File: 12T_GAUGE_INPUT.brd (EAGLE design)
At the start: 70.8 x 63.2 mm, 111 parts, among them P1_WP 10k, P2_WP 10k, P3_WP 10k

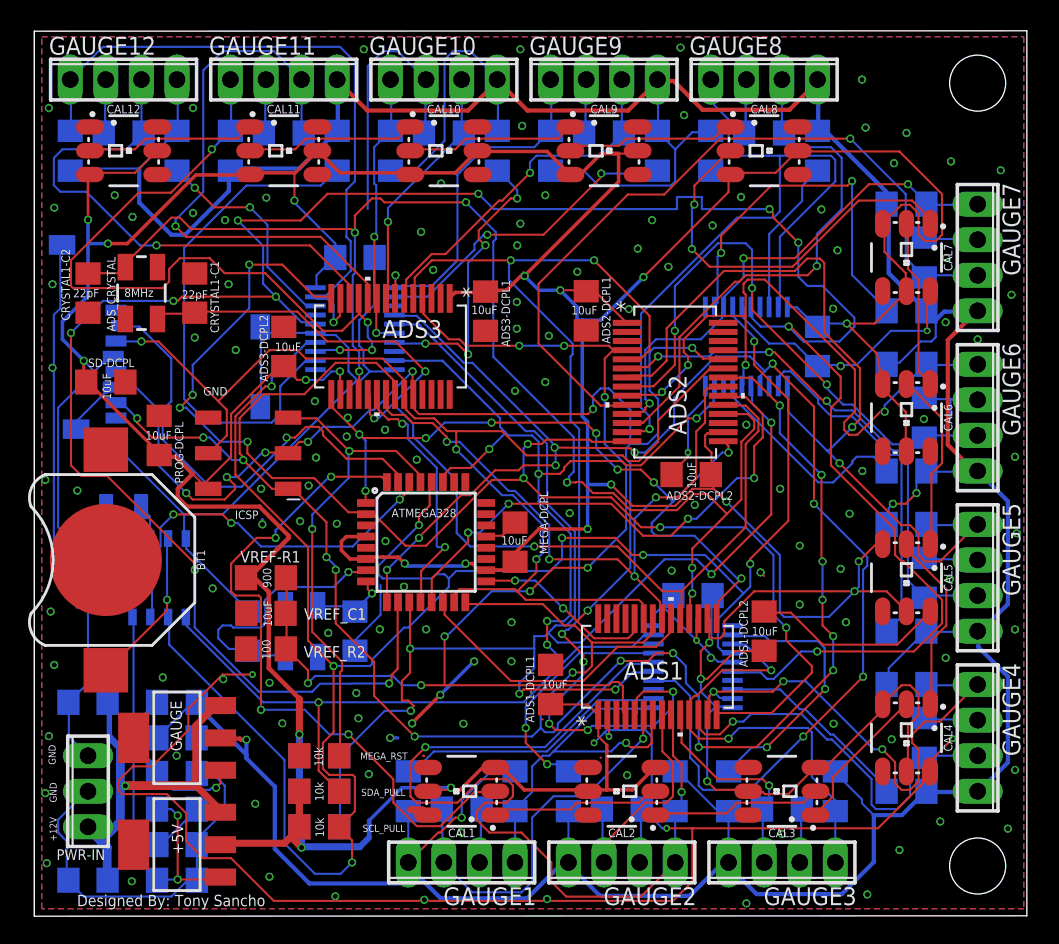
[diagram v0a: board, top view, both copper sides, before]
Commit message: Readability, and made board smaller (again)
Schematic: Moved things around to make it more easily read

Board: Moved things around to shrink the board and increase the ground plane area
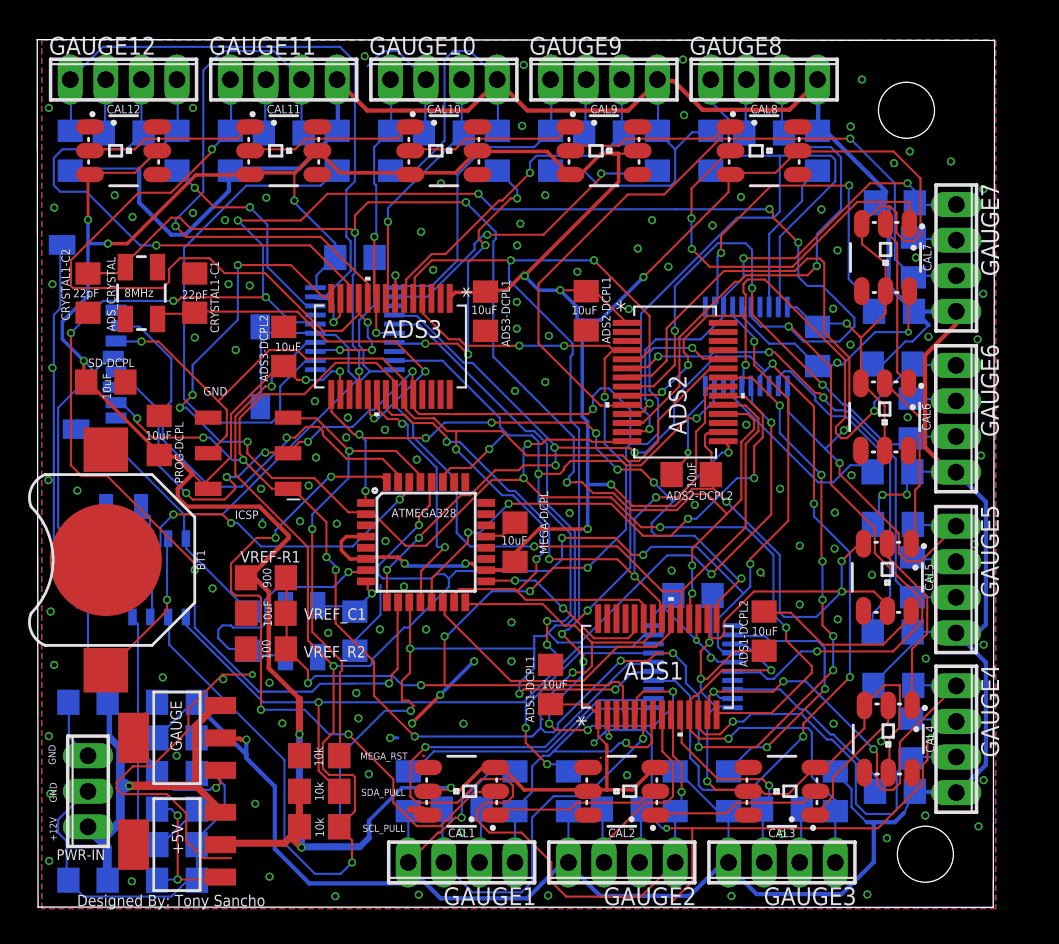
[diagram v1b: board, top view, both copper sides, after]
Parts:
- moved CAL6 1.56 mm to (60.7, 35.6)
- moved GAUGE5 1.55 mm to (65.8, 24.0)
- moved GAUGE6 1.54 mm to (65.8, 35.5)
- moved GAUGE4 1.53 mm to (65.8, 12.6)
- moved GAUGE7 1.52 mm to (65.8, 47.0)
- moved CAL7 1.49 mm to (60.7, 47.0)
- moved CAL5 1.37 mm to (60.9, 24.2)
- moved CAL4 1.30 mm to (60.9, 12.6)
- moved B6-R2 1.00 mm to (61.2, 31.7)
- moved B5-R2 0.99 mm to (61.2, 20.3)
- moved B6R3 0.98 mm to (61.2, 39.4)
- moved B4-R1 0.97 mm to (62.5, 12.7)
- moved B5R3 0.97 mm to (61.3, 27.9)
- moved B6-R1 0.94 mm to (62.6, 35.5)
- moved B4R3 0.94 mm to (61.3, 16.4)
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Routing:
- net GND: track 372.1 -> 316.9 mm, vias 133 -> 136
- net +5V: track 479.6 -> 474.4 mm
- net POT_SELECT_1: track 178.9 -> 174.2 mm
- net B4-_P1W3: track 36.0 -> 33.4 mm
- net B5-_P2W0: track 60.1 -> 57.6 mm
- net B5+: track 38.1 -> 36.4 mm
- net +12V: track 30.0 -> 31.6 mm
- net B6+: track 41.5 -> 39.9 mm
- net P2B1: track 15.6 -> 14.3 mm
- net POT_SELECT_0: track 106.0 -> 105.0 mm
- net B7+: track 55.0 -> 54.0 mm
- net P2B2: track 26.5 -> 25.7 mm
- net B6-_P2W1: track 47.2 -> 46.4 mm
- net P2B0: track 25.2 -> 24.3 mm
- net N$13: track 28.6 -> 27.8 mm
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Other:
- board size 70.8 x 63.2 mm -> 68.3 x 61.9 mm

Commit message: Optimized wire routing
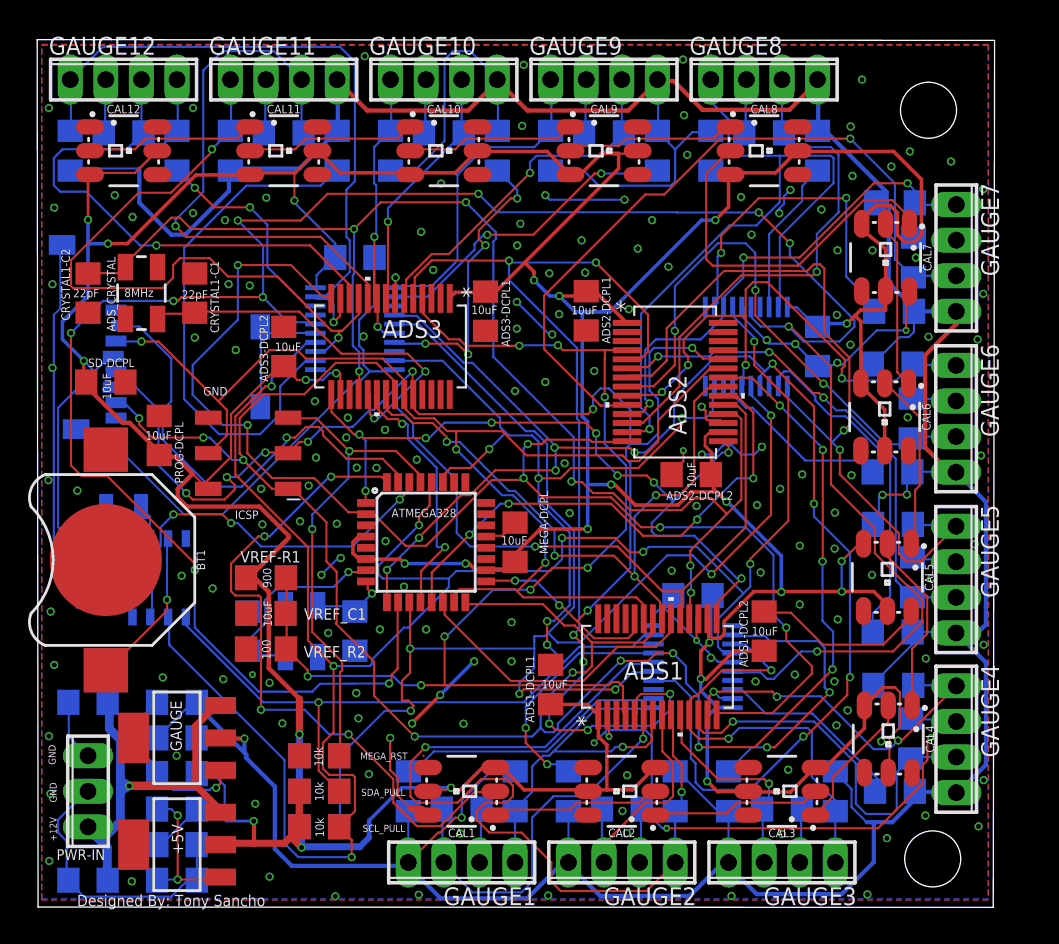
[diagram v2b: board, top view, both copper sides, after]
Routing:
- net GND: track 316.9 -> 266.5 mm, vias 136 -> 166
- net +5V: track 474.4 -> 456.4 mm, vias 23 -> 25
- net B6-_P2W1: track 46.4 -> 39.1 mm
- net B4-_P1W3: track 33.4 -> 27.4 mm
- net B11-_P3W2: track 53.7 -> 49.3 mm, vias 4 -> 2
- net MEGA_XTAL1: track 19.5 -> 15.1 mm
- net V+: track 320.3 -> 316.7 mm
- net XTAL2: track 98.0 -> 95.3 mm
- net SCL: track 151.2 -> 149.5 mm
- net N$13: track 27.8 -> 26.1 mm, vias 2 -> 0
- net AINCOM: track 77.1 -> 75.6 mm
- net P2B2: track 25.7 -> 24.2 mm
- net B5-_P2W0: track 57.6 -> 56.4 mm
- net POT_SELECT_1: track 174.2 -> 172.9 mm
- net XTAL1: track 76.6 -> 75.5 mm
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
